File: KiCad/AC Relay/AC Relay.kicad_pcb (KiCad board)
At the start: 2 copper layers, 49.5 x 49.5 mm, 17 parts, among them J1 Screw_Terminal_01x02, J2 Conn_01x06_Female, J3 Screw_Terminal_01x02, K1 1461492-2, Q1 FDN537N, SW1 SW_Push, U1 BU33SD5WG-TR, U2 ESP-12E, U3 HLK-PM01

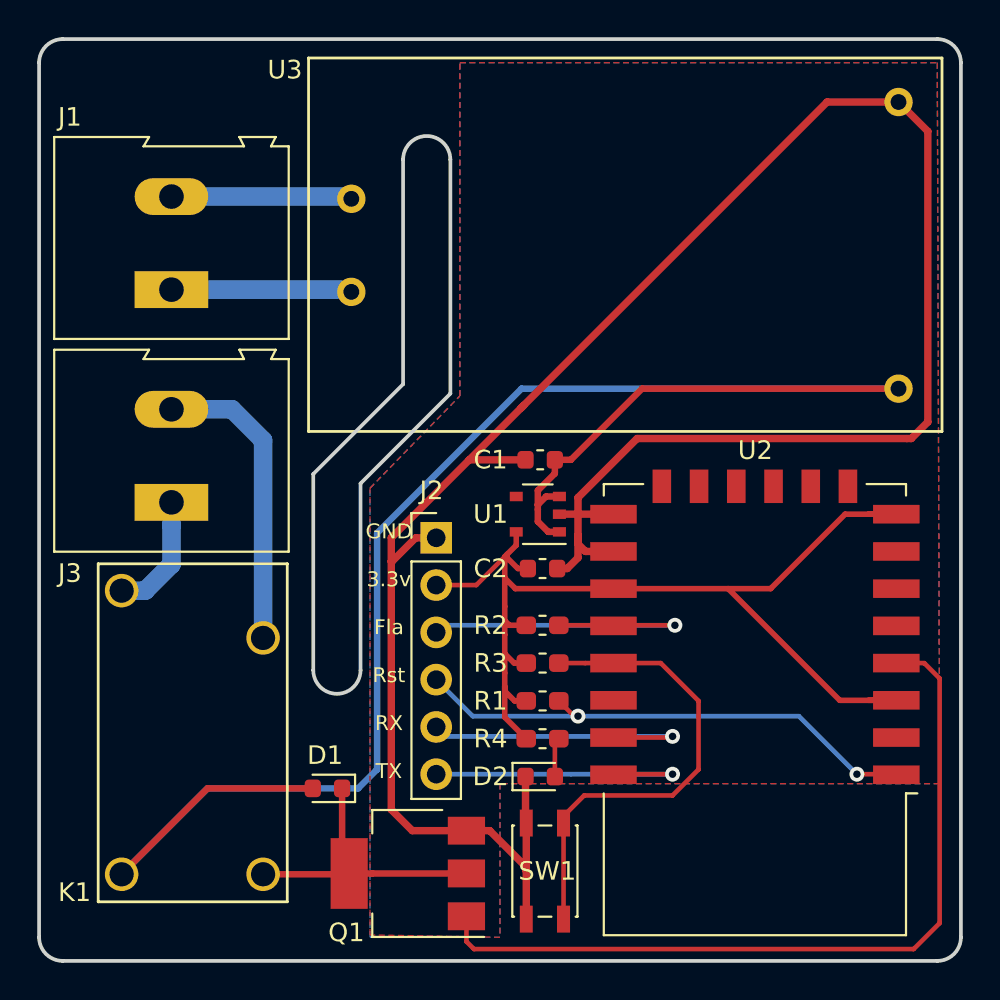
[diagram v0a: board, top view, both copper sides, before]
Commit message: Silk screen and bigger solder surface
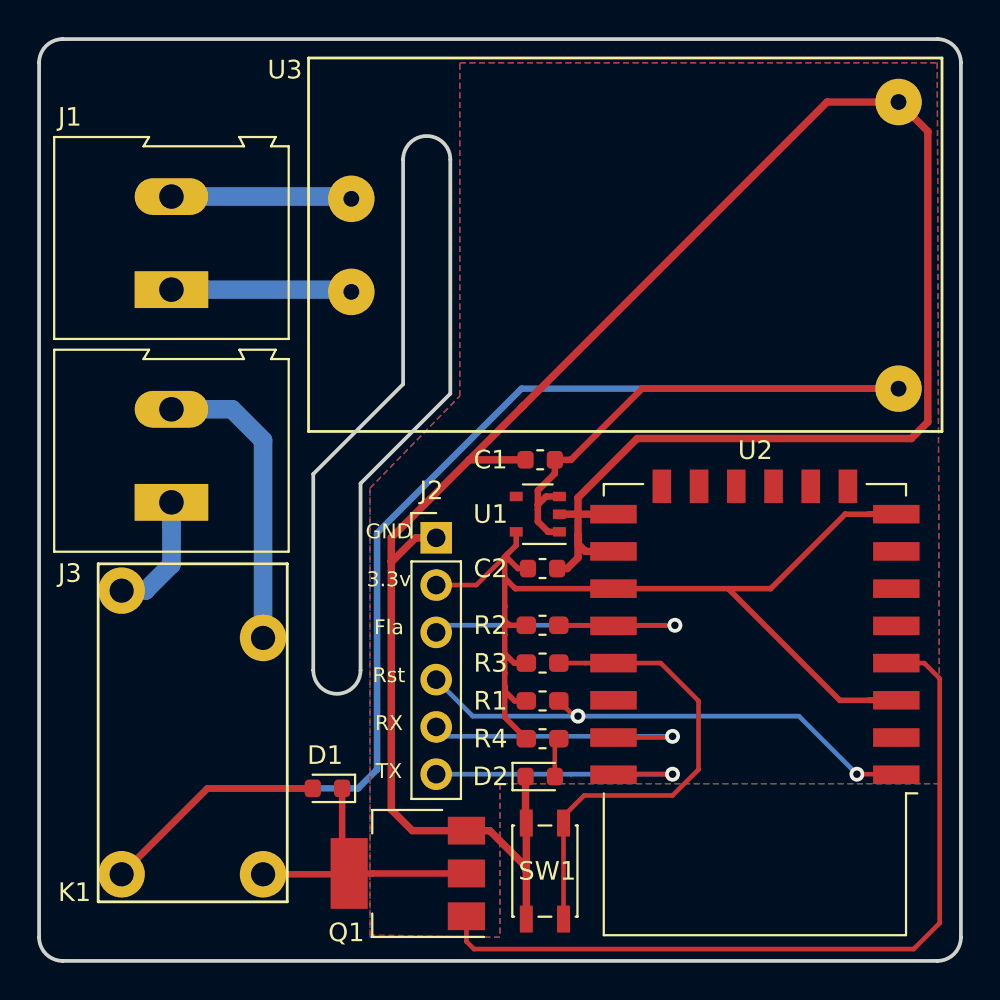
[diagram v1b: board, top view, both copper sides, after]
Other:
- board text added: "AC Relay - ESP8266 Design by Enrique Gómez CC BY-SA 4.0 www.rinconingenieril.es Rev.: 3 - S/N:"
- board text added: "AC in"
- board text added: "Relay"
- board text removed: "AC Relay - ESP8266 Design by Enrique Gómez CC BY-SA 4.0 www.rinconingenieril.es Rev.: 2.1 - S/N:"
